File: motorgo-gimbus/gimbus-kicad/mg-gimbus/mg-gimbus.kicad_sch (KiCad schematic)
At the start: 38 parts, among them CN1 HC-PH-6AWT, CN2 HC-PH-6AWT, J1 motorUVW, SW1 SW_MEC_5G, SW2 2.54-1P TPGT, SW3 SW_MEC_5G, U1 TJA1051TK/3/1J, U2 FSUSB42UMX-TP, U3 ESP32-S3-WROOM-1-N8, U4 FSUSB42UMX-TP, U5 SXL1509-3.3E1, U6 MT6701QT-STD_C2913974, U7 PAM2401YPADJ

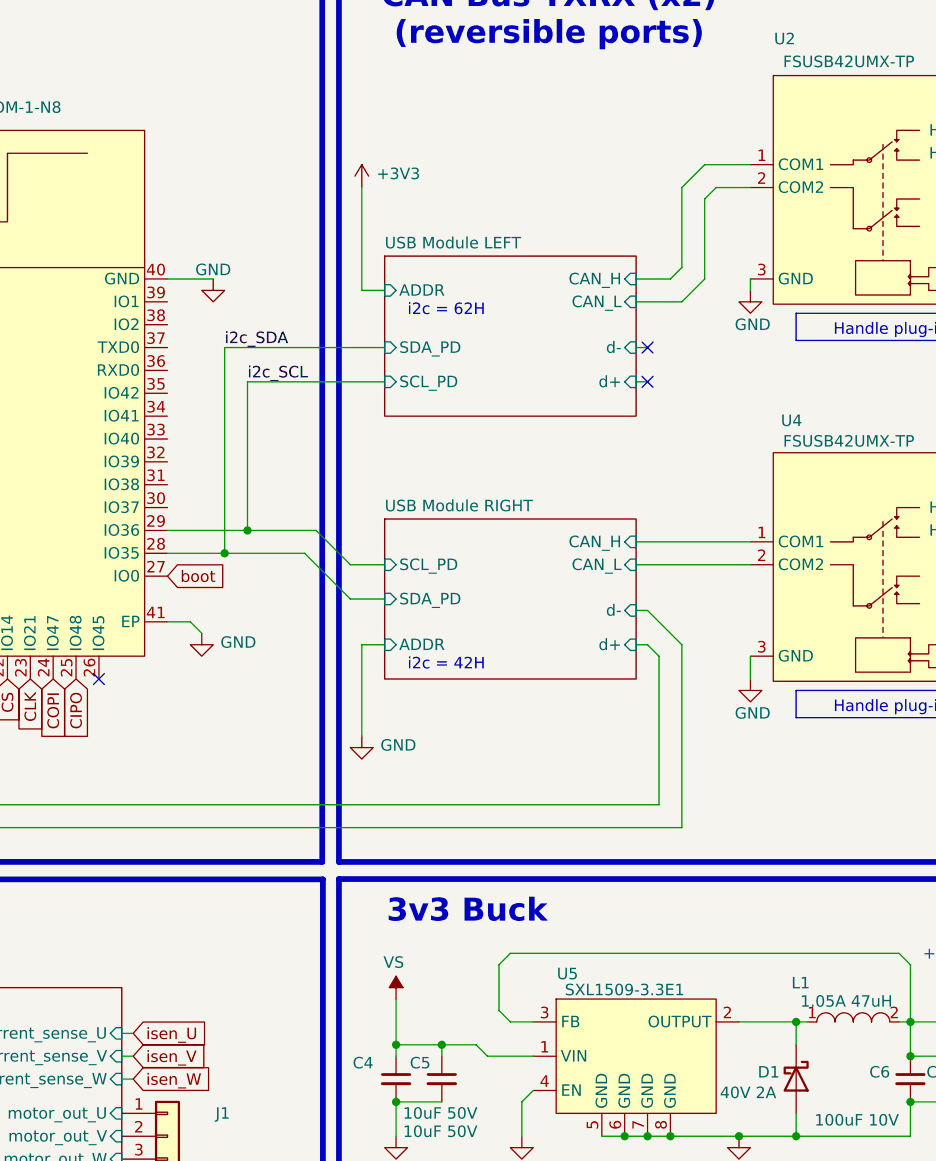
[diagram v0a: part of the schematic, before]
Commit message: update motor controls schema
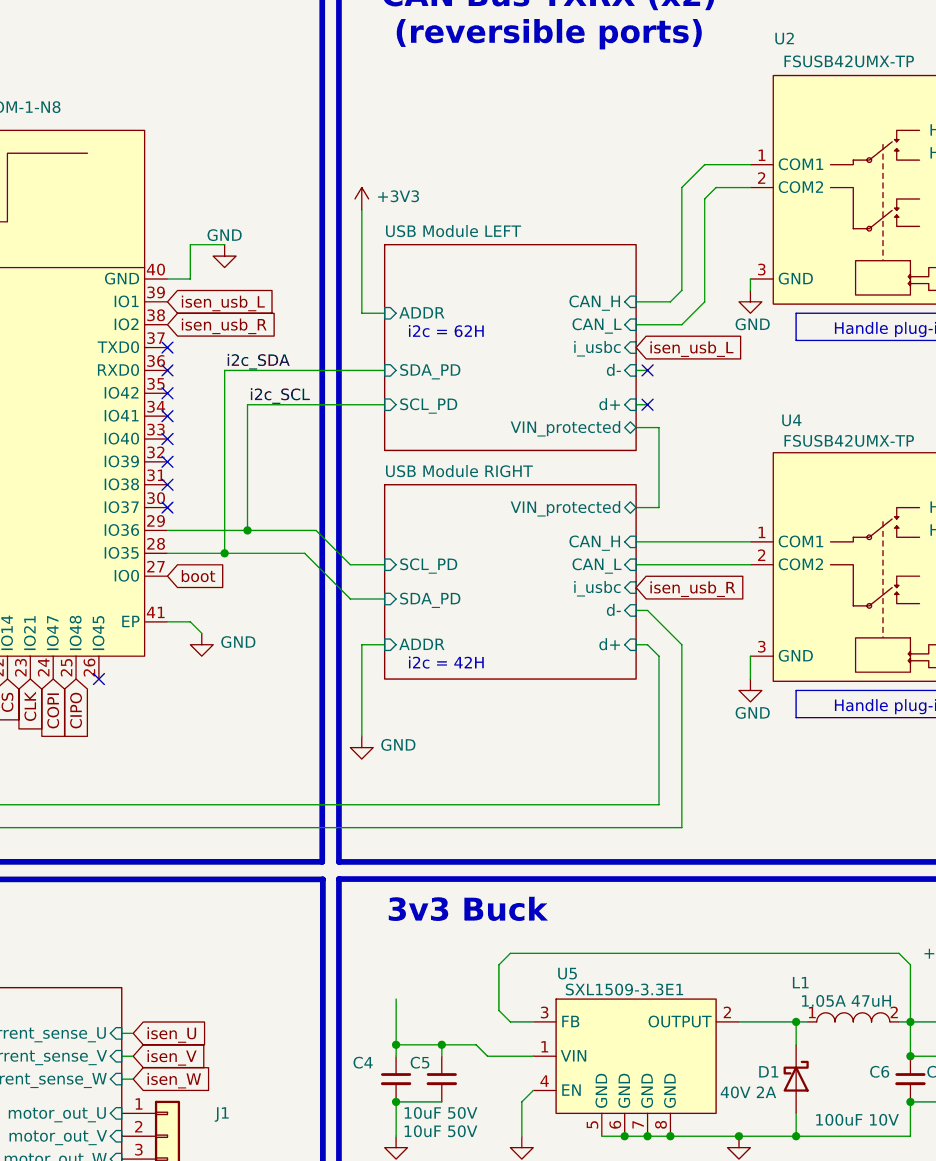
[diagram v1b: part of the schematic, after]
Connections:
- net i2c_SCL: no longer U3.29 (IO36)
- net i2c_SDA: no longer U3.28 (IO35)
- net isen_usb_R: now reaches U3.38 (IO2)
- net isen_usb_L: now reaches U3.39 (IO1)
- net VS: no longer names the net of C4.1, C5.1, U5.1 (VIN)
- new net USB Module LEFT/SCL_PD: U3.29 (IO36)
- new net USB Module LEFT/SDA_PD: U3.28 (IO35)
- no-connect marks 19 -> 27
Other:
- sheet USB Module LEFT ports: added VIN_protected, i_usbc; removed none
- sheet USB Module RIGHT ports: added VIN_protected, i_usbc; removed none

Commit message: incremental layout progress
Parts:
- C1, C2, C3: value 100nF 10v -> 100nF 50V X7R; LCSC Part C309458 -> C152814
- C10, C7: value 47uF 25v -> 47uF 16V; footprint Capacitor_SMD:C_0805_2012Metric -> Capacitor_SMD:C_1206_3216Metric; LCSC Part C16780 -> C172351
- C4, C5: footprint Capacitor_SMD:C_0805_2012Metric -> Capacitor_SMD:C_1206_3216Metric
- C8: value .1uF -> 100nF 50V X7R; footprint (none) -> Capacitor_SMD:C_0402_1005Metric; LCSC Part (none) -> C152814
- C9: value 10uF -> 10uF 50V; footprint Capacitor_SMD:C_0805_2012Metric -> Capacitor_SMD:C_1206_3216Metric
- D1: value 40V 2A -> 30V 2A; footprint gimbus-parts:SOD-123_L2.8-W1.8-LS3.7-RD-2 -> Diode_SMD:D_0603_1608Metric; LCSC Part (none) -> C35621074
- J1: LCSC Part (none) -> n/a
- R1, R4: value 5kΩ -> 5.1KΩ; LCSC Part (none) -> C25905
- R10, R2, R24, R5, R9: LCSC Part (none) -> C25741
- R3: value 90Ω -> 90.9Ω; footprint (none) -> Resistor_SMD:R_0402_1005Metric; LCSC Part (none) -> C208954
- R6, R7: value 5KΩ -> 5.1KΩ; footprint (none) -> Resistor_SMD:R_0402_1005Metric; LCSC Part (none) -> C25905
- R8: LCSC Part (none) -> C43291
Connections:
- net USB Module LEFT/SCL_PD is gone; now on net i2c_SCL: U3.29 (IO36)
- net USB Module LEFT/SDA_PD is gone; now on net i2c_SDA: U3.28 (IO35)
- net +3V3: now also C8.2; no longer C8.1
- net CAN_RX: now also U3.30 (IO37)
- net CAN_TX: now also U3.31 (IO38)
- net GND: now also C8.1; no longer C8.2
- net USB Module LEFT/CAN_H: now also U4.1 (COM1); no longer U2.1 (COM1)
- net USB Module LEFT/CAN_L: now also U4.2 (COM2); no longer U2.2 (COM2)
- net USB Module RIGHT/CAN_H: now also U2.1 (COM1); no longer U4.1 (COM1)
- net USB Module RIGHT/CAN_L: now also U2.2 (COM2); no longer U4.2 (COM2)
- net VBUS: now also C4.1, C5.1, U5.1 (VIN)
- no-connect marks 27 -> 25
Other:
- note added: "Magnetic Encoder"
- note added: "Motor Controls"
- note removed: "MT6701"
- company: (none) -> MotorGo LLC
- title: (none) -> MotorGo Gimbus
- moved on the sheet: D2, R6

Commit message: Ready for ordering pcb files
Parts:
- removed SW2: 2.54-1P TPGT, gimbus-parts:SW-SMD_2P-L6.2-W2.5-LS9.4, symbol gimbus-parts:2.54-1PTPGT
- added R42, R43: 5.1KΩ, Resistor_SMD:R_0402_1005Metric, symbol Device:R_Small_US
- added U15: HX MINI MSK12CO2, gimbus-parts:SW-SMD_MSK12CO2, symbol gimbus-parts:HXMINIMSK12CO2
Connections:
- net +3V3: now also R42.1, R43.1
- net CAN_Flip_Left: now also R5.2, U4.10 (SEL); no longer R2.2, U2.10 (SEL)
- net CAN_Flip_Right: now also R2.2, U2.10 (SEL); no longer R5.2, U4.10 (SEL)
- net GND: now also U15.4, U15.5
- net i2c_SCL: now also R42.2
- net i2c_SDA: now also R43.2
- net isen_U: now also U3.5 (IO5); no longer U3.4 (IO4)
- net isen_V: now also U3.4 (IO4); no longer U3.5 (IO5)
- net at U1.6 (CANL), U2.4 (HSD1-), U2.7 (HSD2+)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: now also U15.1
- net at R3.2: now also U15.2, U15.3
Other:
- sheet USB Module LEFT ports: added none; removed VIN_protected
- sheet USB Module RIGHT ports: added none; removed VIN_protected
- note added: "Toggle"
- note removed: "DIP"
